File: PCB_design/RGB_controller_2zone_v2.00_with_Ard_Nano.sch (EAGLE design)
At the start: 25 parts, among them Q1 IRF512, Q2 IRF512, Q3 IRF512, Q4 IRF512, Q5 IRF512, Q6 IRF512

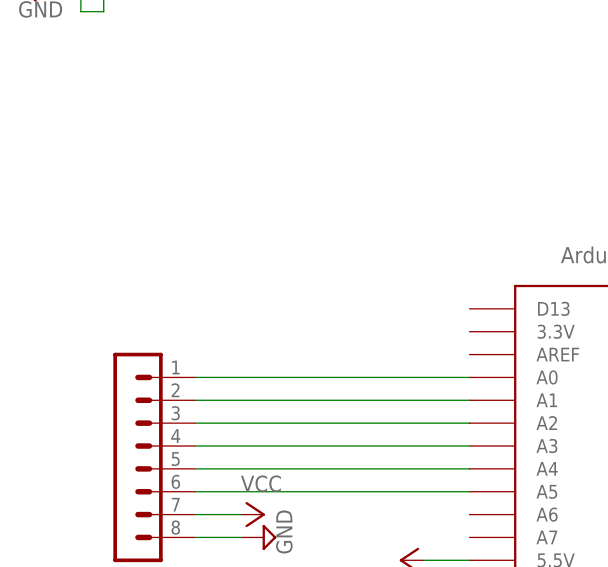
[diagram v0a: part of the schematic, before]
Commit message: Update PCB for using arduino nano
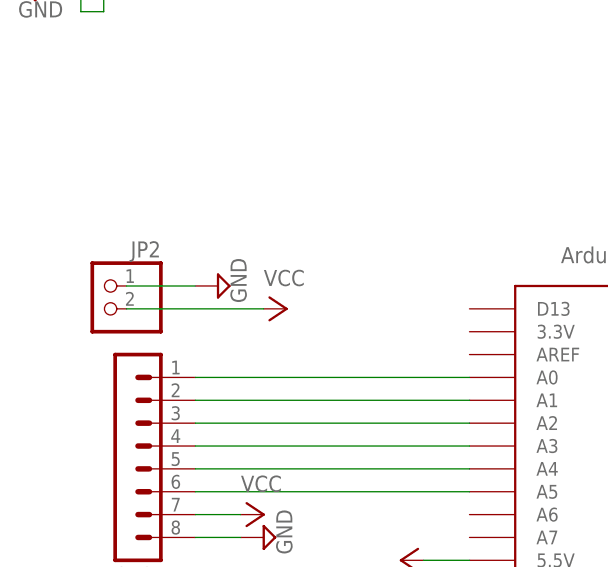
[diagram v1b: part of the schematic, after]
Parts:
- added JP2: (no value), pinhead:PINHD-1X2
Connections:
- net GND: now also JP2.1
- net VCC: now also JP2.2
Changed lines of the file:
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@@
 <part name="JP1" library="pinhead" deviceset="PINHD-1X2" device=""/>
 <part name="SUPPLY7" library="supply2" deviceset="GND" device=""/>
+<part name="JP2" library="pinhead" deviceset="PINHD-1X2" device=""/>
+<part name="P+3" library="supply1" deviceset="VCC" device=""/>
+<part name="SUPPLY9" library="supply2" deviceset="GND" device=""/>
 </parts>
 <sheets>
@@
 <instance part="JP1" gate="G$1" x="96.52" y="66.04"/>
 <instance part="SUPPLY7" gate="GND" x="93.98" y="63.5"/>
+<instance part="JP2" gate="G$1" x="0" y="58.42" rot="MR0"/>
+<instance part="P+3" gate="VCC" x="20.32" y="58.42" rot="R270"/>
+<instance part="SUPPLY9" gate="GND" x="12.7" y="60.96" rot="R90"/>
 </instances>
 <busses>
@@
 <pinref part="JP1" gate="G$1" pin="2"/>
 <pinref part="SUPPLY7" gate="GND" pin="GND"/>
+</segment>
+<segment>
+<pinref part="JP2" gate="G$1" pin="1"/>
+<pinref part="SUPPLY9" gate="GND" pin="GND"/>
+<wire x1="10.16" y1="60.96" x2="2.54" y2="60.96" width="0.1524" layer="91"/>
 </segment>
 </net>
@@
 <wire x1="10.16" y1="35.56" x2="15.24" y2="35.56" width="0.1524" layer="91"/>
 </segment>
-</net>
+<segment>
+<pinref part="JP2" gate="G$1" pin="2"/>
+<pinref part="P+3" gate="VCC" pin="VCC"/>
+<wire x1="17.78" y1="58.42" x2="2.54" y2="58.42" width="0.1524" layer="91"/>
+</segment>
+</net>
